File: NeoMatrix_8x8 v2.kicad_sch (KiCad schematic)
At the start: 140 parts

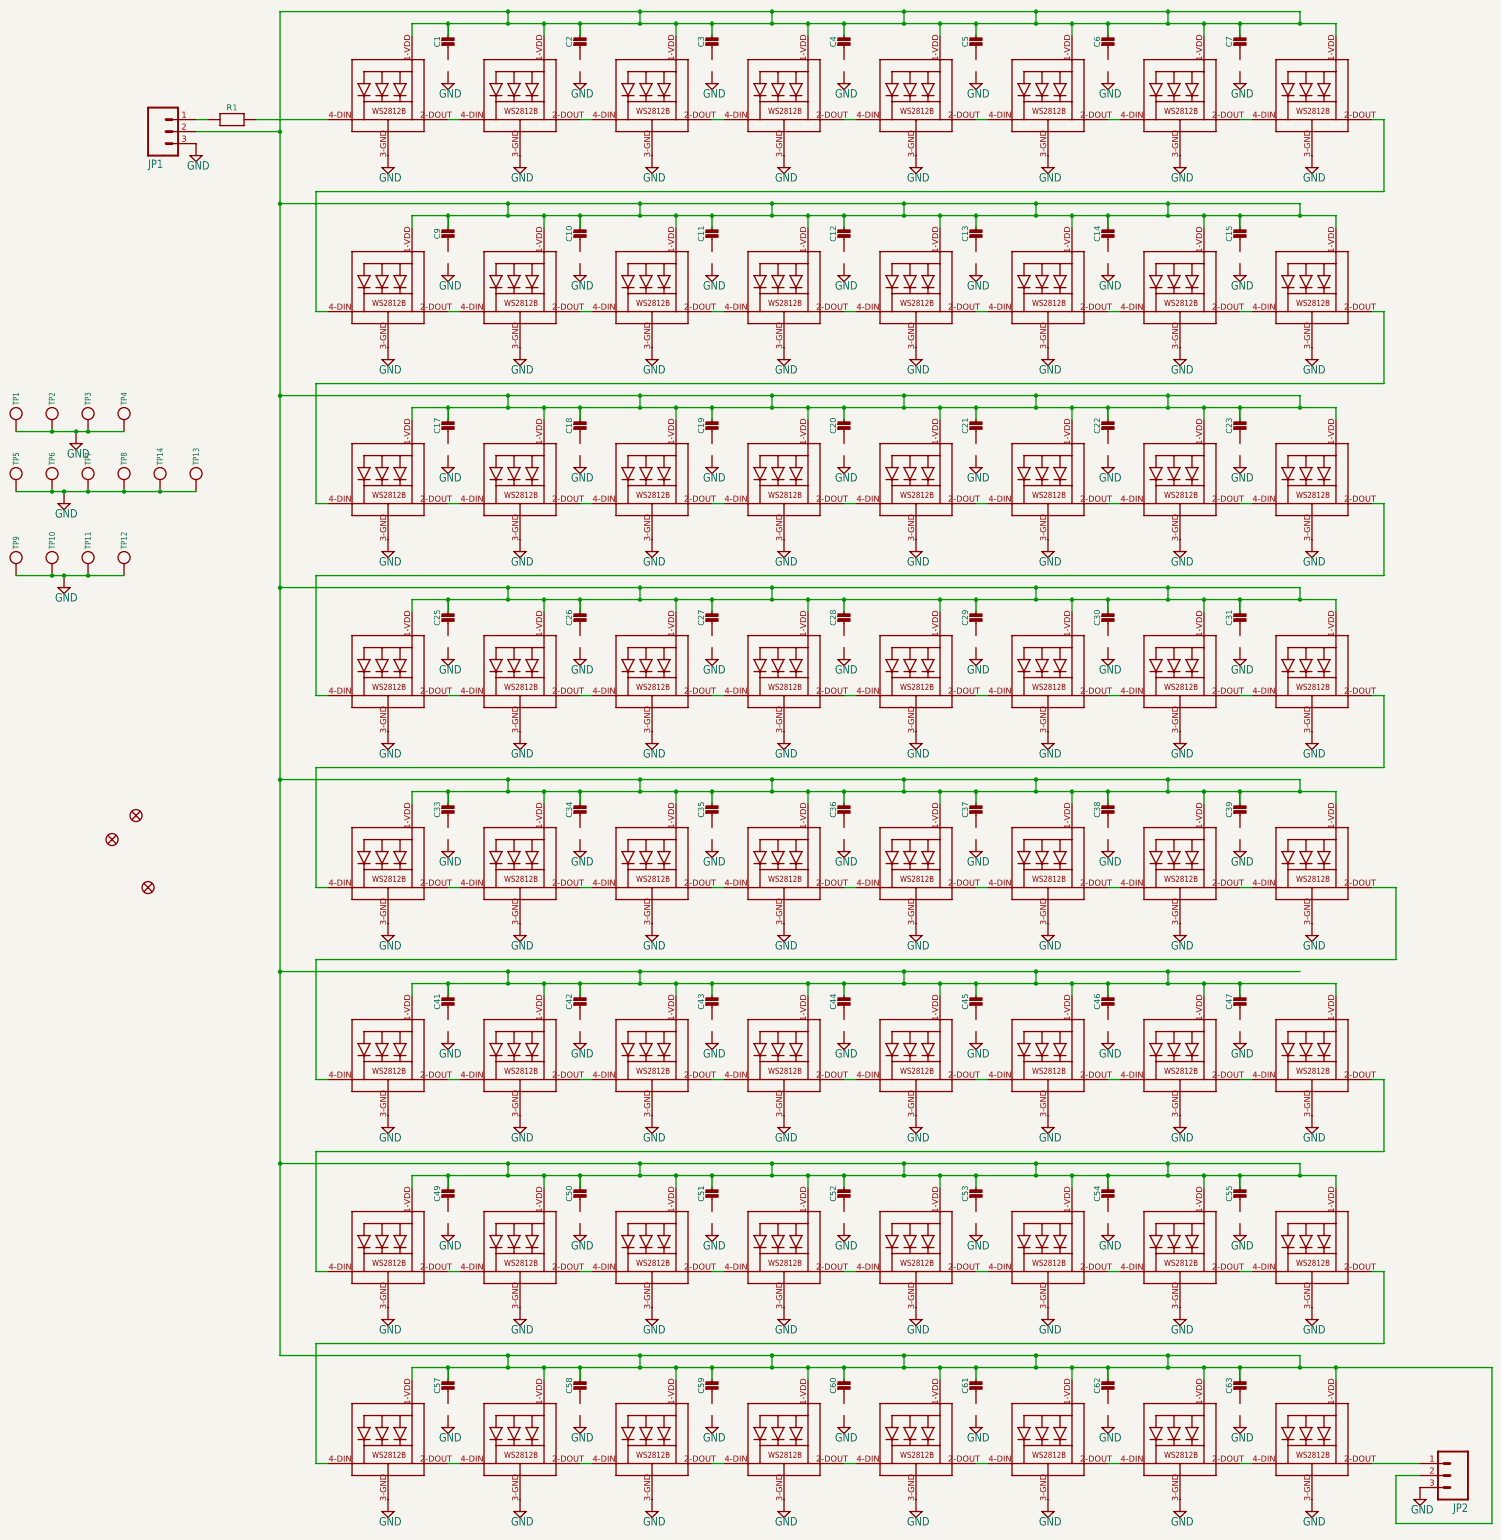
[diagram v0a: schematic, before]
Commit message: Modified schematic to use blocks
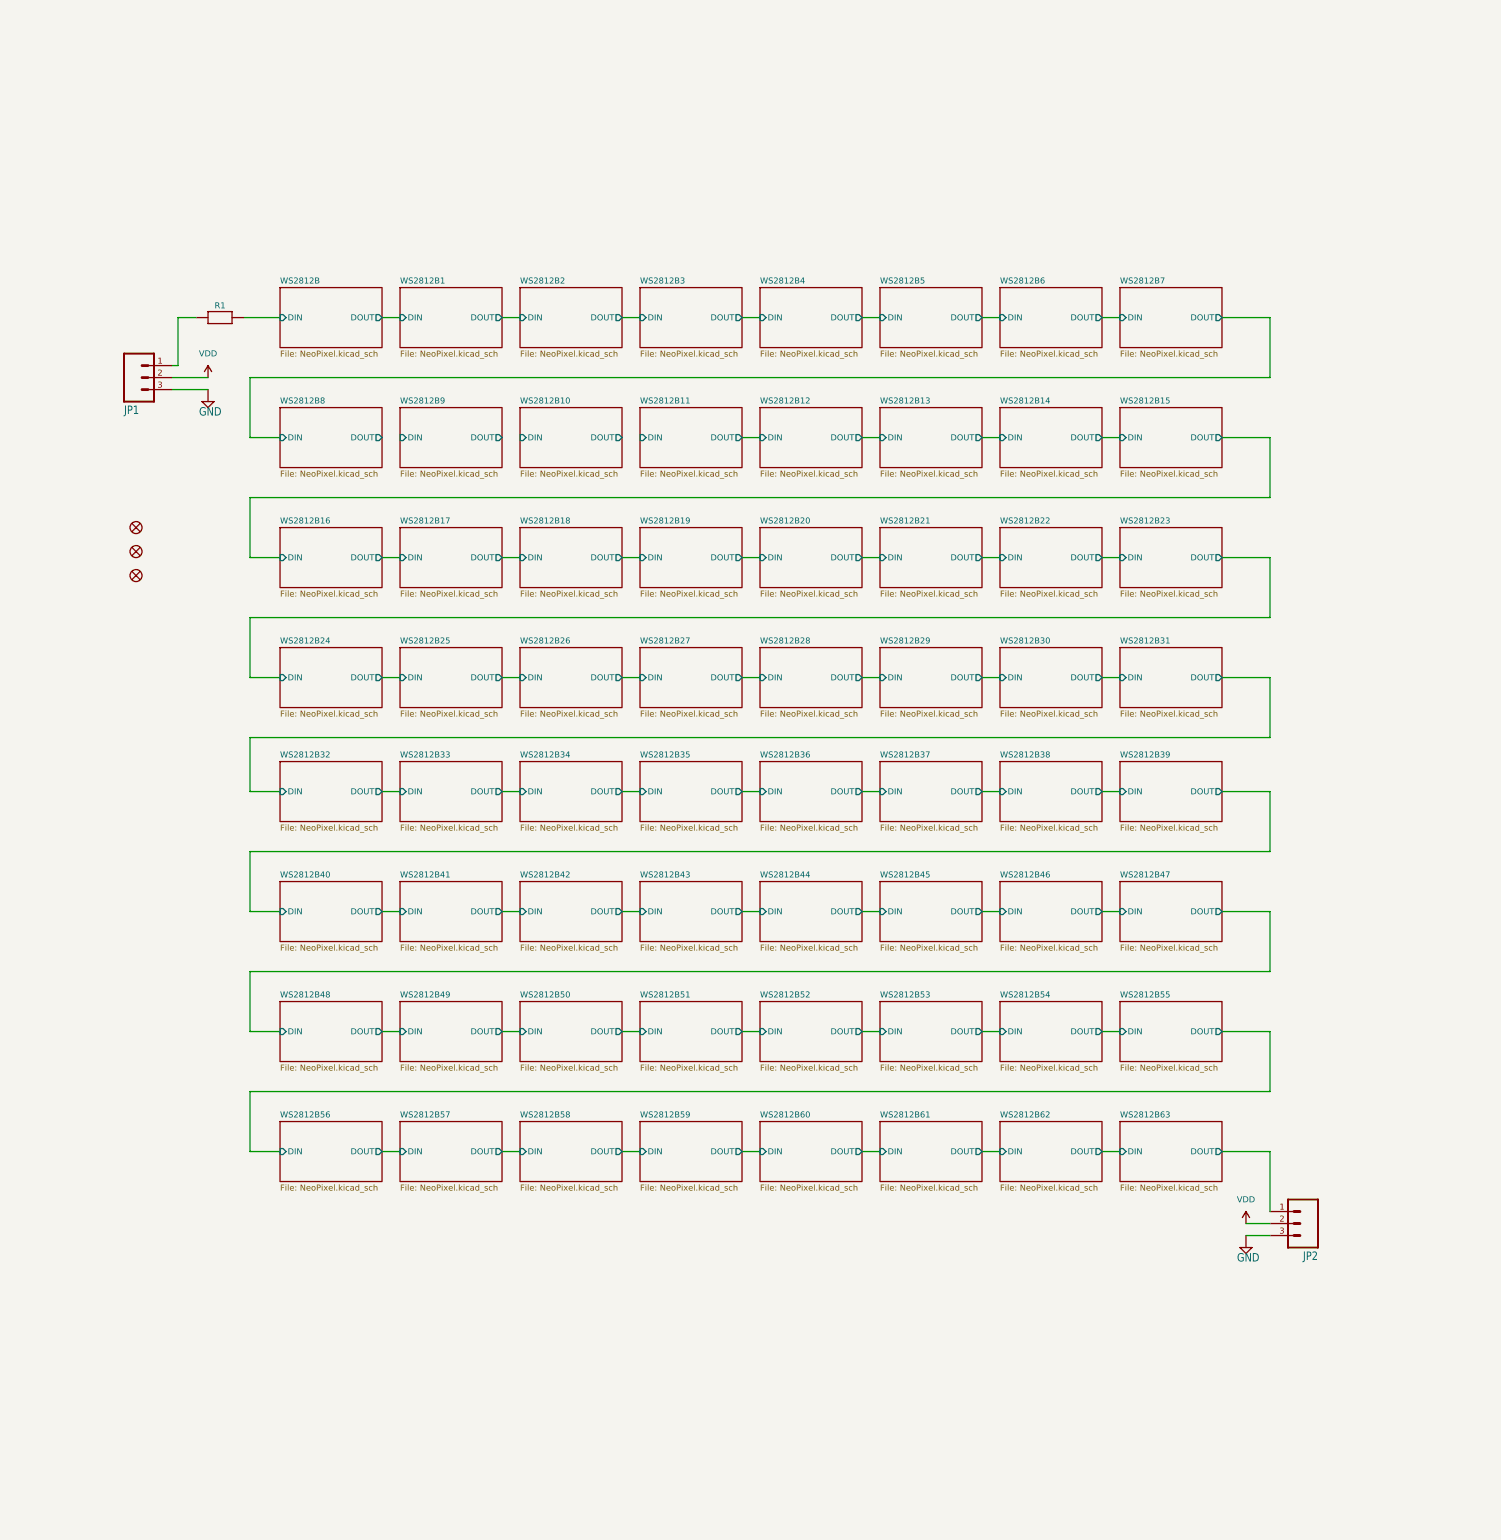
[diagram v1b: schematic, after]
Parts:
- removed C1, C10, C11, C12, C13, C14, C15, C17, C18, C19, C2, C20, C21, C22, C23, C25, C26, C27, C28, C29, C3, C30, C31, C33, C34, C35, C36, C37, C38, C39, C4, C41, C42, C43, C44, C45, C46, C47, C49, C5, C50, C51, C52, C53, C54, C55, C57, C58, C59, C6, C60, C61, C62, C63, C7, C9: CAP_CERAMIC0805-NOOUTLINE, Adafruit_NeoMatrix_8x8 v2:0805-NO, symbol Adafruit_NeoMatrix_8x8 v2-eagle-import:CAP_CERAMIC0805-NOOUTLINE
- removed LED1, LED10, LED11, LED12, LED13, LED14, LED15, LED16, LED17, LED18, LED19, LED2, LED20, LED21, LED22, LED23, LED24, LED25, LED26, LED27, LED28, LED29, LED3, LED30, LED31, LED32, LED33, LED34, LED35, LED36, LED37, LED38, LED39, LED4, LED40, LED41, LED42, LED43, LED44, LED45, LED46, LED47, LED48, LED49, LED5, LED50, LED51, LED52, LED53, LED54, LED55, LED56, LED57, LED58, LED59, LED6, LED60, LED61, LED62, LED63, LED64, LED7, LED8, LED9: WS2812B5050, Adafruit_NeoMatrix_8x8 v2:WS2812B, symbol Adafruit_NeoMatrix_8x8 v2-eagle-import:WS2812B5050
- removed TP1, TP10, TP11, TP12, TP13, TP14, TP2, TP3, TP4, TP5, TP6, TP7, TP8, TP9: TESTPOINT, Adafruit_NeoMatrix_8x8 v2:TESTPOINT_SMT, symbol Adafruit_NeoMatrix_8x8 v2-eagle-import:TESTPOINT
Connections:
- net VDD: now reaches JP1.2, JP2.2
- net WS2812B/DIN: now reaches R1.2
- net WS2812B63/DOUT: now reaches JP2.1
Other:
- added sheet WS2812B (NeoPixel.kicad_sch)
- added sheet WS2812B1 (NeoPixel.kicad_sch)
- added sheet WS2812B10 (NeoPixel.kicad_sch)
- added sheet WS2812B11 (NeoPixel.kicad_sch)
- added sheet WS2812B12 (NeoPixel.kicad_sch)
- added sheet WS2812B13 (NeoPixel.kicad_sch)
- added sheet WS2812B14 (NeoPixel.kicad_sch)
- added sheet WS2812B15 (NeoPixel.kicad_sch)
- added sheet WS2812B16 (NeoPixel.kicad_sch)
- added sheet WS2812B17 (NeoPixel.kicad_sch)
- added sheet WS2812B18 (NeoPixel.kicad_sch)
- added sheet WS2812B19 (NeoPixel.kicad_sch)
- added sheet WS2812B2 (NeoPixel.kicad_sch)
- added sheet WS2812B20 (NeoPixel.kicad_sch)
- added sheet WS2812B21 (NeoPixel.kicad_sch)
- added sheet WS2812B22 (NeoPixel.kicad_sch)
- added sheet WS2812B23 (NeoPixel.kicad_sch)
- added sheet WS2812B24 (NeoPixel.kicad_sch)
- added sheet WS2812B25 (NeoPixel.kicad_sch)
- added sheet WS2812B26 (NeoPixel.kicad_sch)
- added sheet WS2812B27 (NeoPixel.kicad_sch)
- added sheet WS2812B28 (NeoPixel.kicad_sch)
- added sheet WS2812B29 (NeoPixel.kicad_sch)
- added sheet WS2812B3 (NeoPixel.kicad_sch)
- added sheet WS2812B30 (NeoPixel.kicad_sch)
- added sheet WS2812B31 (NeoPixel.kicad_sch)
- added sheet WS2812B32 (NeoPixel.kicad_sch)
- added sheet WS2812B33 (NeoPixel.kicad_sch)
- added sheet WS2812B34 (NeoPixel.kicad_sch)
- added sheet WS2812B35 (NeoPixel.kicad_sch)
- added sheet WS2812B36 (NeoPixel.kicad_sch)
- added sheet WS2812B37 (NeoPixel.kicad_sch)
- added sheet WS2812B38 (NeoPixel.kicad_sch)
- added sheet WS2812B39 (NeoPixel.kicad_sch)
- added sheet WS2812B4 (NeoPixel.kicad_sch)
- added sheet WS2812B40 (NeoPixel.kicad_sch)
- added sheet WS2812B41 (NeoPixel.kicad_sch)
- added sheet WS2812B42 (NeoPixel.kicad_sch)
- added sheet WS2812B43 (NeoPixel.kicad_sch)
- added sheet WS2812B44 (NeoPixel.kicad_sch)
- added sheet WS2812B45 (NeoPixel.kicad_sch)
- added sheet WS2812B46 (NeoPixel.kicad_sch)
- added sheet WS2812B47 (NeoPixel.kicad_sch)
- added sheet WS2812B48 (NeoPixel.kicad_sch)
- added sheet WS2812B49 (NeoPixel.kicad_sch)
- added sheet WS2812B5 (NeoPixel.kicad_sch)
- added sheet WS2812B50 (NeoPixel.kicad_sch)
- added sheet WS2812B51 (NeoPixel.kicad_sch)
- added sheet WS2812B52 (NeoPixel.kicad_sch)
- added sheet WS2812B53 (NeoPixel.kicad_sch)
- added sheet WS2812B54 (NeoPixel.kicad_sch)
- added sheet WS2812B55 (NeoPixel.kicad_sch)
- added sheet WS2812B56 (NeoPixel.kicad_sch)
- added sheet WS2812B57 (NeoPixel.kicad_sch)
- added sheet WS2812B58 (NeoPixel.kicad_sch)
- added sheet WS2812B59 (NeoPixel.kicad_sch)
- added sheet WS2812B6 (NeoPixel.kicad_sch)
- added sheet WS2812B60 (NeoPixel.kicad_sch)
- added sheet WS2812B61 (NeoPixel.kicad_sch)
- added sheet WS2812B62 (NeoPixel.kicad_sch)
- added sheet WS2812B63 (NeoPixel.kicad_sch)
- added sheet WS2812B7 (NeoPixel.kicad_sch)
- added sheet WS2812B8 (NeoPixel.kicad_sch)
- added sheet WS2812B9 (NeoPixel.kicad_sch)
- moved on the sheet: JP1, JP2, R1

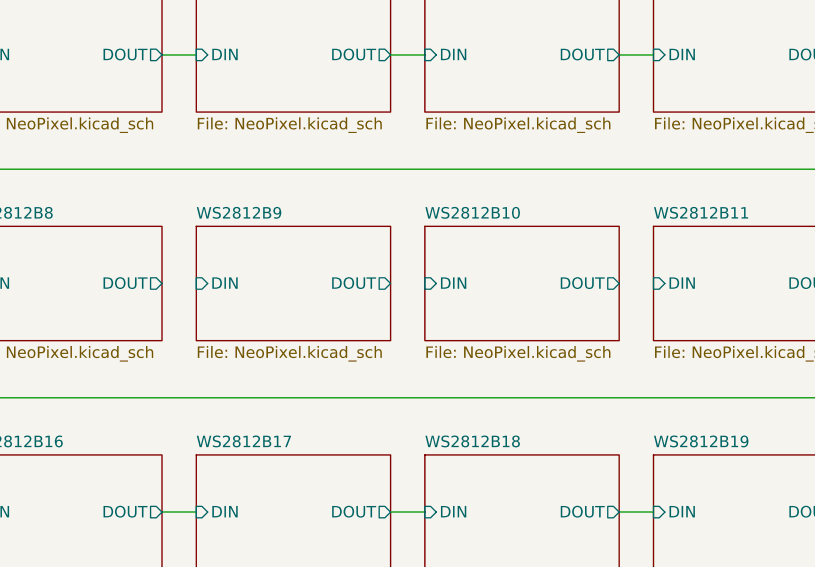
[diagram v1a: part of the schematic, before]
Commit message: Libraries corrected, references updated
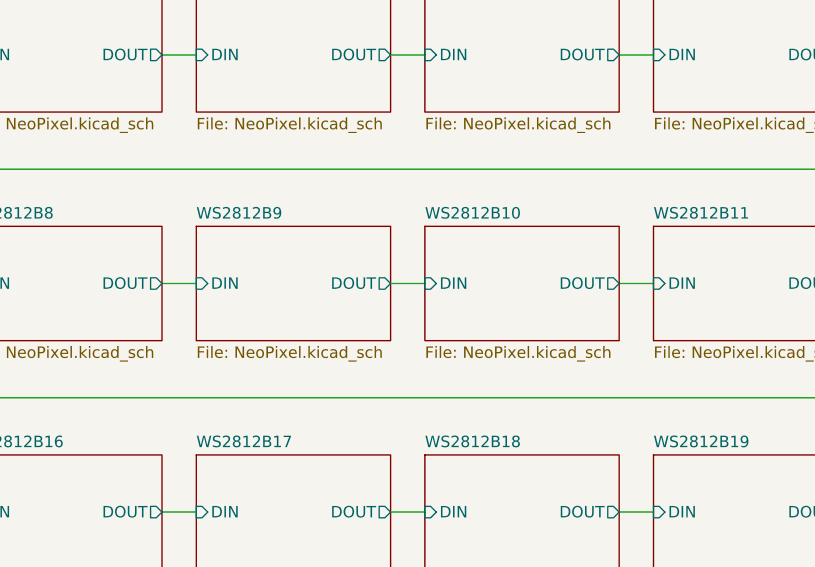
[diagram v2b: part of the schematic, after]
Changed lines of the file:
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@@
+	(wire
+		(pts
+			(xy 123.19 107.95) (xy 127 107.95)
+		)
+		(stroke
+			(width 0)
+			(type default)
+		)
+	)
 	(wire
 		(pts
@@
 		(pts
 			(xy 123.19 208.28) (xy 127 208.28)
+		)
+		(stroke
+			(width 0)
+			(type default)
+		)
+	)
+	(wire
+		(pts
+			(xy 97.79 107.95) (xy 101.6 107.95)
 		)
 		(stroke
@@
 		)
 		(stroke
+			(width 0)
+			(type default)
+		)
+	)
+	(wire
+		(pts
+			(xy 148.59 107.95) (xy 152.4 107.95)
+		)
+		(stroke

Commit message: Revised mounting holes and layout
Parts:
- R1: value RESISTOR0805_NOOUTLINE -> 470R
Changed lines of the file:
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@@
 			)
 		)
-		(property "Value" "RESISTOR0805_NOOUTLINE"
+		(property "Value" "470R"
 			(at 63.5 82.55 0)
 			(effects
